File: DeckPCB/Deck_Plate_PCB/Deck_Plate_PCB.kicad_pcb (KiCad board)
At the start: 2 copper layers, 119.2 x 99.1 mm, 60 parts, among them J1 Raspberry_Pi_2_3, J2 NASA_Telemetry_Interface, J3 NASA PWR_Interface, J8 Board_to_Board, J9 Power, P1 Digital, P10 CONN_01X01, P11 CONN_01X01, P12 CONN_01X01, P13 CONN_01X01, P2 Power, P3 Analog, P4 Analog, P5 PWM, P6 PWM, P7 Communication, P8 CONN_01X01, P9 CONN_01X01, Q2 2N7000, Q3 2N7000, U1 D24V25F9, U2 LM2576T-5, U3 D24V25F9, U5 LM2576T-5, U6 SF_Logic_Level_Conv, U7 Lidar_RangeFinder, U8 ADXL377

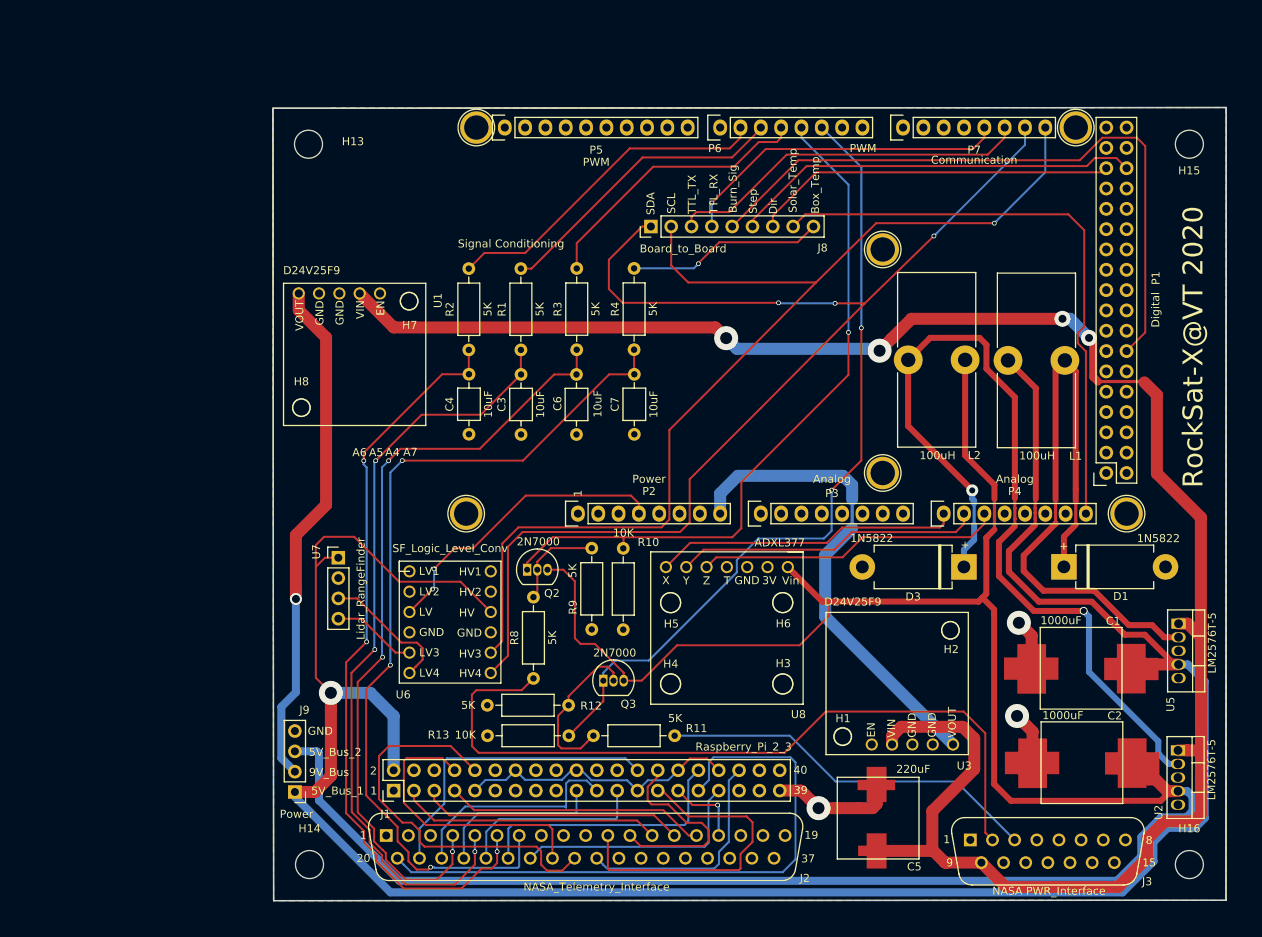
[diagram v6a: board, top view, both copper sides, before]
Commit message: Updated Main_Board and Daughter_Board to have rounded off corners to fit inside of the Electronics Enclosure. Verified with CAD model of electronics enclosure.
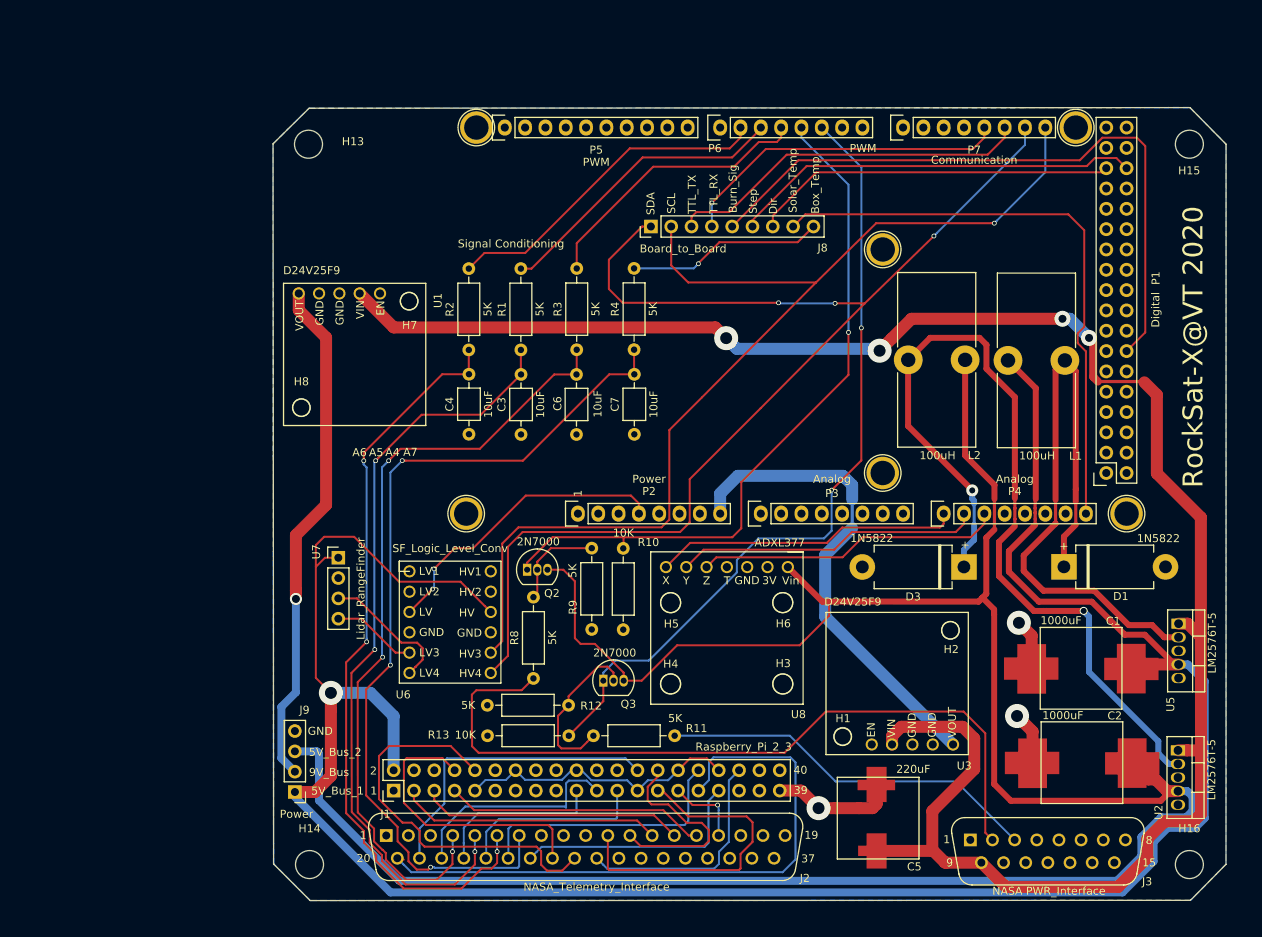
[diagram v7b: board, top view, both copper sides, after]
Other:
- board size 119.2 x 99.1 mm -> 119.1 x 99.1 mm
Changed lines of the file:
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@@
       (psa4output false)
       (plotreference true)
-      (plotvalue false)
+      (plotvalue true)
       (plotinvisibletext false)
       (padsonsilk false)
@@
       (net 36 "Net-(P13-Pad1)"))
   )
+  (gr_line (start 200.55 50.98) (end 200.54 140.99) (layer Edge.Cuts) (width 0.15))
+  (gr_line (start 85.93 46.48) (end 196.04 46.4) (layer Edge.Cuts) (width 0.15))
+  (gr_line (start 81.49 140.95) (end 81.42 50.93) (layer Edge.Cuts) (width 0.15))
+  (gr_line (start 196.1 145.49) (end 86.06 145.52) (layer Edge.Cuts) (width 0.15))
+  (gr_line (start 196.1 145.49) (end 200.54 140.99) (layer Edge.Cuts) (width 0.15))
+  (gr_line (start 86.06 145.52) (end 81.49 140.95) (layer Edge.Cuts) (width 0.15))
+  (gr_line (start 81.42 50.93) (end 85.93 46.48) (layer Edge.Cuts) (width 0.15))
+  (gr_line (start 196.04 46.4) (end 200.55 50.98) (layer Edge.Cuts) (width 0.15))
   (gr_text + (at 167.93 101.05) (layer F.SilkS)
     (effects (font (size 1 1) (thickness 0.25)))
   )
-  (gr_line (start 81.49 145.53) (end 81.41 46.48) (layer Edge.Cuts) (width 0.15))
-  (gr_line (start 200.54 145.49) (end 81.49 145.53) (layer Edge.Cuts) (width 0.15))
-  (gr_line (start 200.56 46.39) (end 200.54 145.49) (layer Edge.Cuts) (width 0.15))
-  (gr_line (start 81.41 46.48) (end 200.56 46.39) (layer Edge.Cuts) (width 0.15))
-  (gr_line (start 200.56 46.39) (end 200.54 145.49) (layer F.SilkS) (width 0.15))
-  (gr_line (start 81.41 46.48) (end 200.56 46.39) (layer F.SilkS) (width 0.15))
-  (gr_line (start 81.49 145.53) (end 81.41 46.49) (layer F.SilkS) (width 0.15))
-  (gr_line (start 200.54 145.49) (end 81.49 145.53) (layer F.SilkS) (width 0.15))
   (gr_text "RockSat-X@VT 2020 Team" (at 98.81 54.43) (layer B.SilkS)
     (effects (font (size 1.5 1.5) (thickness 0.3)) (justify mirror))
@@
     (polygon
       (pts
-        (xy 200.54 145.49) (xy 81.49 145.53) (xy 81.41 46.48) (xy 200.56 46.39)
+        (xy 200.55 50.98) (xy 200.54 140.99) (xy 196.1 145.49) (xy 86.06 145.52) (xy 81.49 140.95)
+        (xy 81.42 50.93) (xy 85.92 46.48) (xy 196.04 46.4)
       )
     )
